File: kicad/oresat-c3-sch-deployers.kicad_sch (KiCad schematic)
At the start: 22 parts, among them Q10 FDMQ86530L, Q11 DMP2240UDM-7, Q5 DMP2240UDM-7, Q7 DMP2240UDM-7, Q8 FDMQ86530L, Q9 DMP2240UDM-7

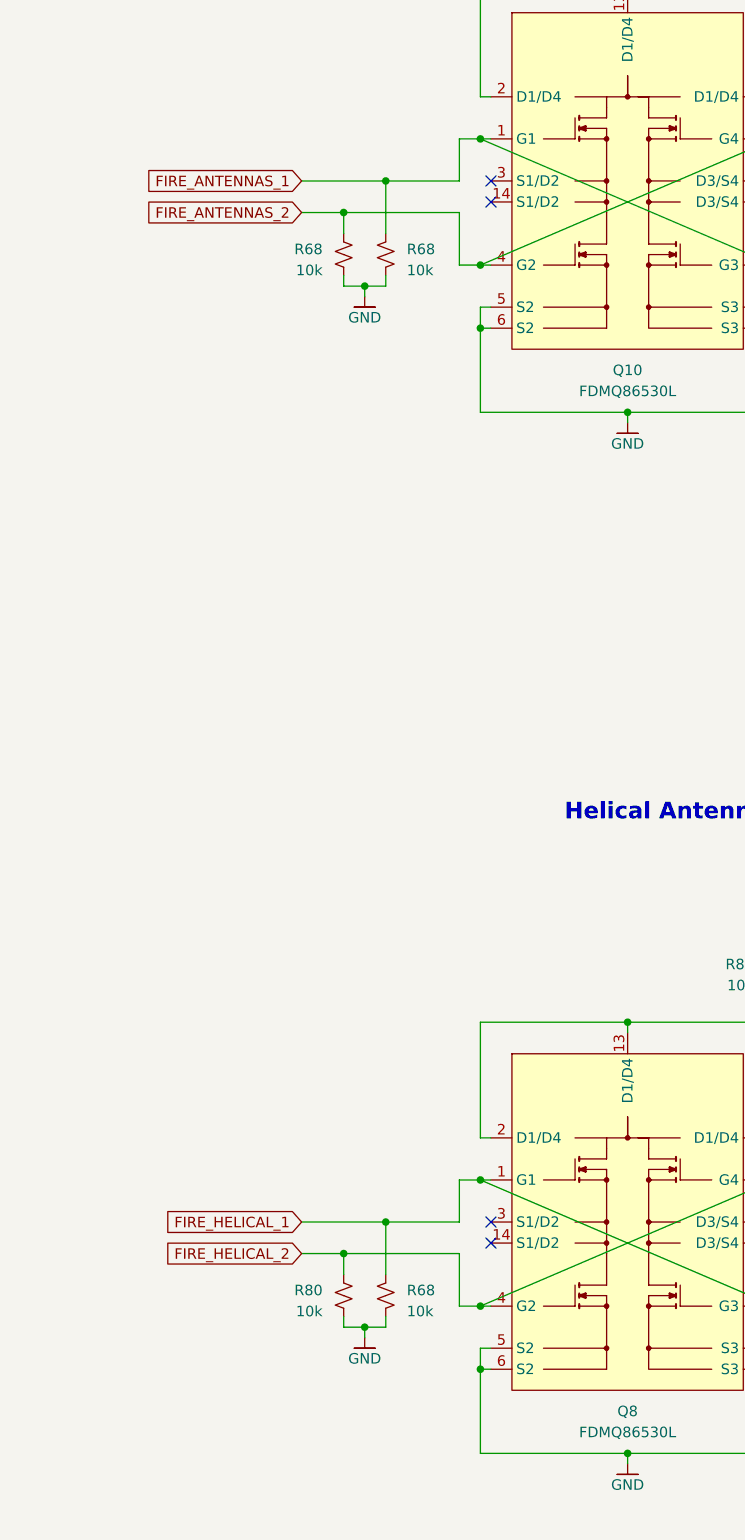
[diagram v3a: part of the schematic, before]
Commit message: Updated test points, fixed some more hidden ERCs.
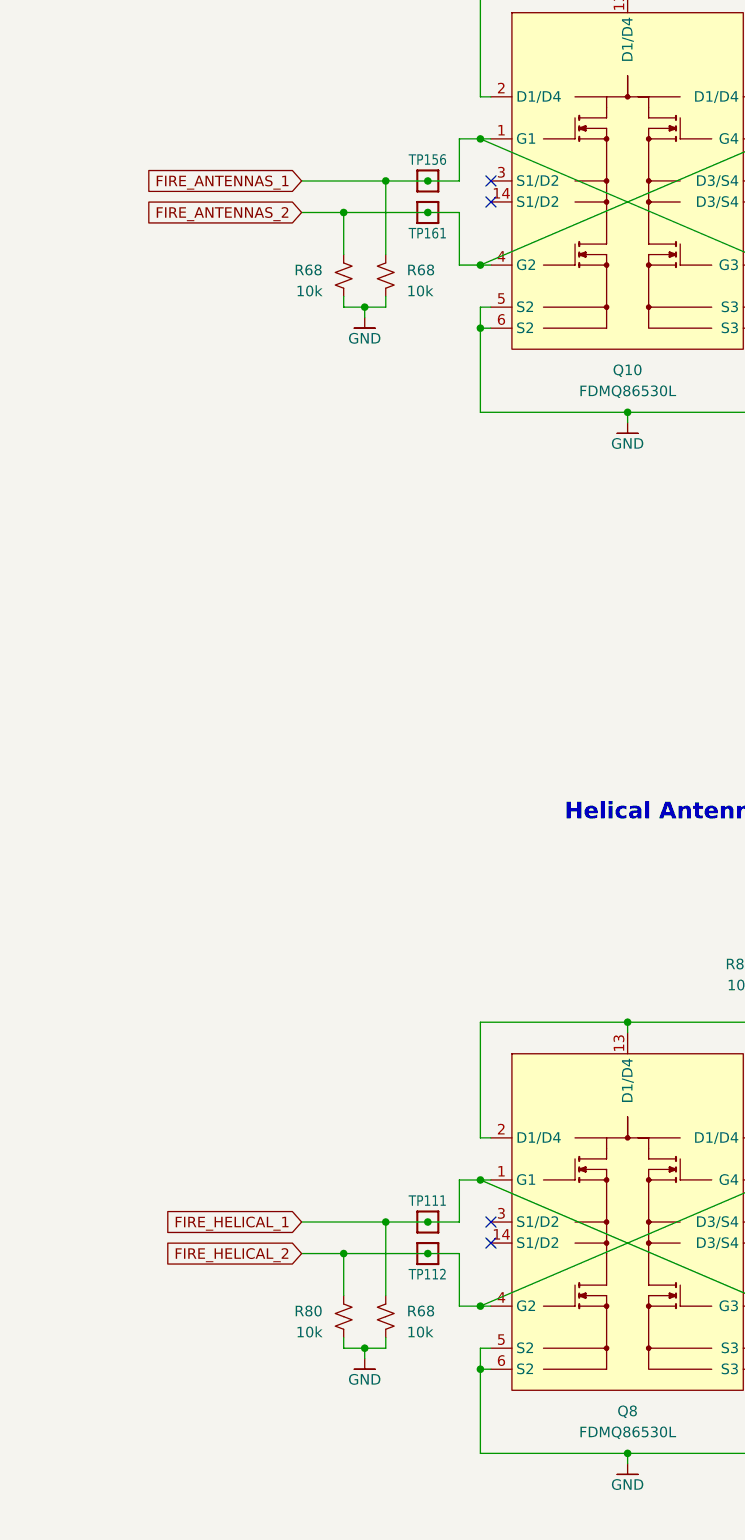
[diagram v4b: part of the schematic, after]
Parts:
- added TP111, TP112, TP156, TP161: Test-Point, TestPoint:TestPoint_Pad_D1.0mm, symbol oresat-misc:Test-Point-1mm-round
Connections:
- net FIRE_ANTENNAS_1: now also TP156.1
- net FIRE_ANTENNAS_2: now also TP161.1
- net FIRE_HELICAL_1: now also TP111.1
- net FIRE_HELICAL_2: now also TP112.1
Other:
- moved on the sheet: R68, R80

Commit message: Fixed test points; added RF test points. Started on layout and component packages for UHF radio.
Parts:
- TP1, TP111, TP112, TP156, TP161, TP3: footprint TestPoint:TestPoint_Pad_D1.0mm -> oresat-misc:TestPoint_Pad_D1.0mm
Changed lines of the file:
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@@
       (effects (font (size 1.27 1.27)) hide)
     )
-    (property "Footprint" "TestPoint:TestPoint_Pad_D1.0mm" (at 270.51 209.55 0)
+    (property "Footprint" "oresat-misc:TestPoint_Pad_D1.0mm" (at 270.51 209.55 0)
       (effects (font (size 1.27 1.27)) hide)
     )
@@
       (effects (font (size 1.27 1.27)) hide)
     )
-    (property "Footprint" "TestPoint:TestPoint_Pad_D1.0mm" (at 179.07 88.9 0)
+    (property "Footprint" "oresat-misc:TestPoint_Pad_D1.0mm" (at 179.07 88.9 0)
       (effects (font (size 1.27 1.27)) hide)
     )
@@
       (effects (font (size 1.27 1.27)) hide)
     )
-    (property "Footprint" "TestPoint:TestPoint_Pad_D1.0mm" (at 179.07 92.71 0)
+    (property "Footprint" "oresat-misc:TestPoint_Pad_D1.0mm" (at 179.07 92.71 0)
       (effects (font (size 1.27 1.27)) hide)
     )
@@
       (effects (font (size 1.27 1.27)) hide)
     )
-    (property "Footprint" "TestPoint:TestPoint_Pad_D1.0mm" (at 179.07 214.63 0)
+    (property "Footprint" "oresat-misc:TestPoint_Pad_D1.0mm" (at 179.07 214.63 0)
       (effects (font (size 1.27 1.27)) hide)
     )
@@
       (effects (font (size 1.27 1.27)) hide)
     )
-    (property "Footprint" "TestPoint:TestPoint_Pad_D1.0mm" (at 278.13 73.66 0)
+    (property "Footprint" "oresat-misc:TestPoint_Pad_D1.0mm" (at 278.13 73.66 0)
       (effects (font (size 1.27 1.27)) hide)
     )
@@
       (effects (font (size 1.27 1.27)) hide)
     )
-    (property "Footprint" "TestPoint:TestPoint_Pad_D1.0mm" (at 179.07 218.44 0)
-      (effects (font (size 1.27 1.27)) hide)
-    )
+    (property "Footprint" "oresat-misc:TestPoint_Pad_D1.0mm" (at 179.07 218.44 0)
+      (effects (font (size 1.27 1.27)) hide)
+    )

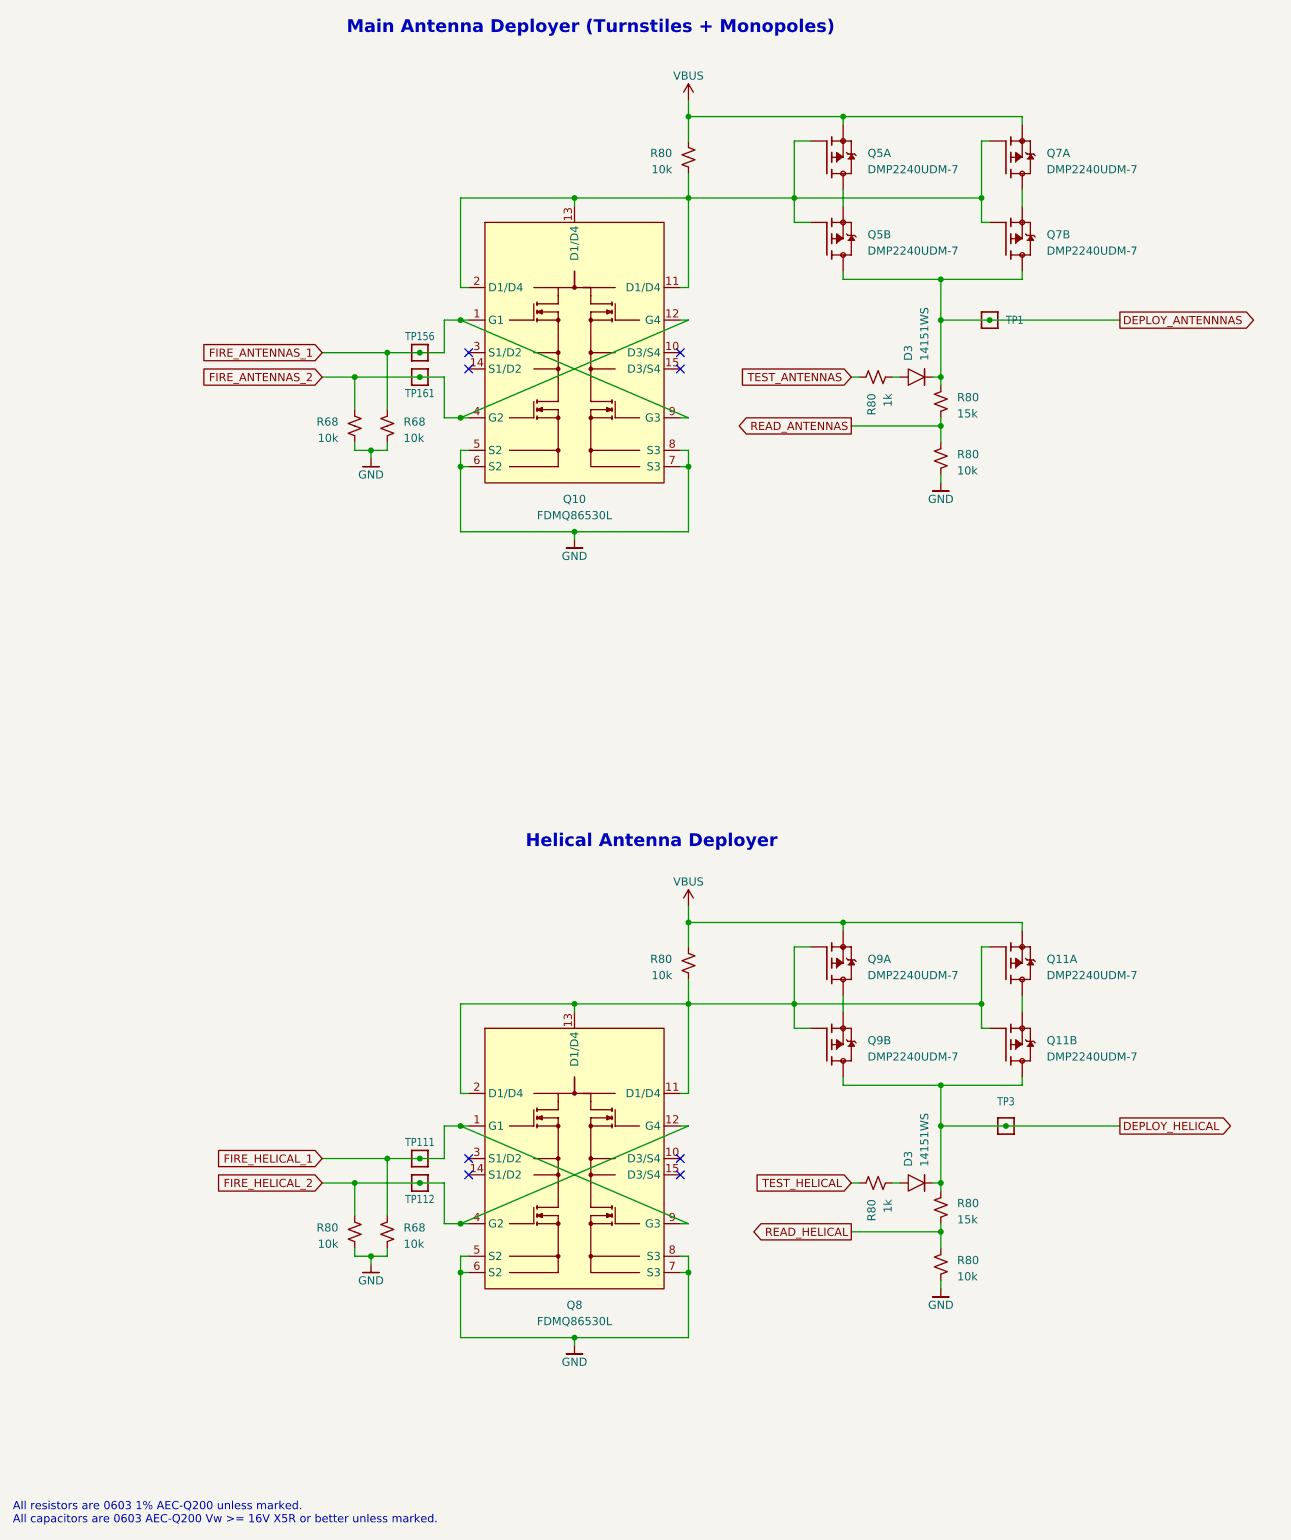
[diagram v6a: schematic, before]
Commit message: Fixed footprints and laid out WDT and OPD circuitry.
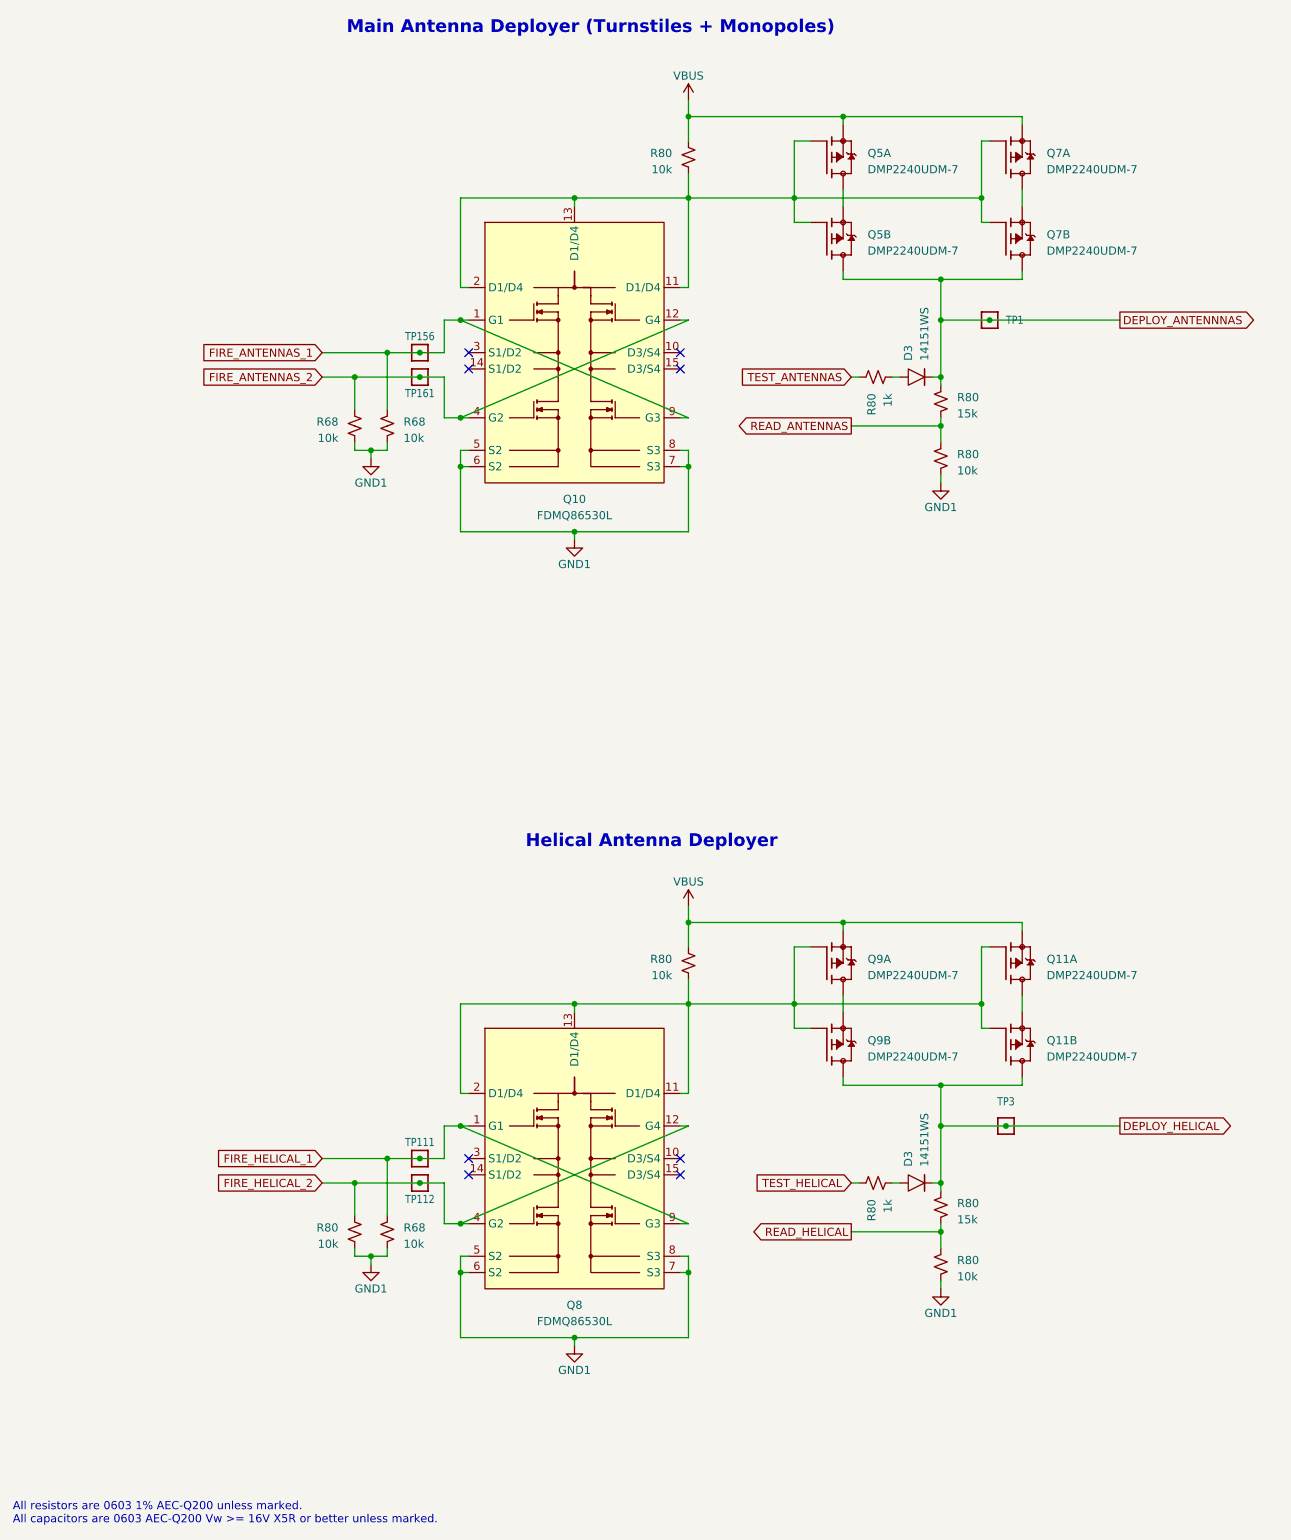
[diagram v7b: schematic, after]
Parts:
- R68, R80: footprint (none) -> Resistor_SMD:R_0603_1608Metric
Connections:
- net DEPLOY_ANTENNNAS: now also D3.1; no longer D3. (2)
- net DEPLOY_HELICAL: now also D3.1; no longer D3. (2)
- net at R80.2: now also D3.2; no longer D3. (2) (x2)
- net GND renamed GND1
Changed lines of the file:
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@@
     )
   )
-  (symbol (lib_id "oresat-power:GND") (at 171.45 95.25 0) (unit 1)
+  (symbol (lib_id "power:GND1") (at 171.45 95.25 0) (unit 1)
     (in_bom yes) (on_board yes) (dnp no)
     (property "Reference" "#GND0163" (at 171.45 101.6 0)
       (effects (font (size 1.27 1.27)) hide)
     )
-    (property "Value" "GND" (at 171.45 97.79 0)
+    (property "Value" "GND1" (at 171.45 99.06 0)
       (effects (font (size 1.27 1.27)))
     )
@@
         )
         (path "/65d12cdd-c326-4033-9053-c59fa4e0b25e/f40986af-661f-42e2-86b8-cadc1b813505"
-          (reference "#GND046") (unit 1)
+          (reference "#PWR0189") (unit 1)
         )
       )
@@
       (effects (font (size 1.27 1.27)) hide)
     )
-    (pin "")
-    (pin "")
+    (pin "1")
+    (pin "2")
     (instances
       (project "oresat-c3"
@@
       (effects (font (size 1.27 1.27)) (justify right))
     )
-    (property "Footprint" "" (at 220.98 173.99 0)
+    (property "Footprint" "Resistor_SMD:R_0603_1608Metric" (at 220.98 173.99 0)
       (effects (font (size 1.27 1.27)) hide)
     )
@@
     )
   )
-  (symbol (lib_id "oresat-power:GND") (at 171.45 220.98 0) (unit 1)
+  (symbol (lib_id "power:GND1") (at 171.45 220.98 0) (unit 1)
     (in_bom yes) (on_board yes) (dnp no)
     (property "Reference" "#GND0163" (at 171.45 227.33 0)
       (effects (font (size 1.27 1.27)) hide)
     )
-    (property "Value" "GND" (at 171.45 223.52 0)
+    (property "Value" "GND1" (at 171.45 224.79 0)
       (effects (font (size 1.27 1.27)))
     )
@@
         )
         (path "/65d12cdd-c326-4033-9053-c59fa4e0b25e/f40986af-661f-42e2-86b8-cadc1b813505"
-          (reference "#GND051") (unit 1)
+          (reference "#PWR0192") (unit 1)
         )
       )
@@
     )
   )
-  (symbol (lib_id "oresat-power:GND") (at 260.35 224.79 0) (unit 1)
+  (symbol (lib_id "power:GND1") (at 260.35 224.79 0) (unit 1)
     (in_bom yes) (on_board yes) (dnp no)
     (property "Reference" "#GND0163" (at 260.35 231.14 0)
       (effects (font (size 1.27 1.27)) hide)
     )
-    (property "Value" "GND" (at 260.35 227.33 0)
+    (property "Value" "GND1" (at 260.35 228.6 0)
       (effects (font (size 1.27 1.27)))
     )
@@
         )
         (path "/65d12cdd-c326-4033-9053-c59fa4e0b25e/f40986af-661f-42e2-86b8-cadc1b813505"
-          (reference "#GND053") (unit 1)
-        )
-      )
-    )
-  )
-  (symbol (lib_id "oresat-power:GND") (at 203.2 107.95 0) (unit 1)
+          (reference "#PWR0191") (unit 1)
+        )
+      )
+    )
+  )
+  (symbol (lib_id "power:GND1") (at 203.2 107.95 0) (unit 1)
     (in_bom yes) (on_board yes) (dnp no)
     (property "Reference" "#GND0163" (at 203.2 114.3 0)
       (effects (font (size 1.27 1.27)) hide)
     )
-    (property "Value" "GND" (at 203.2 110.49 0)
+    (property "Value" "GND1" (at 203.2 111.76 0)
       (effects (font (size 1.27 1.27)))
     )
@@
         )
         (path "/65d12cdd-c326-4033-9053-c59fa4e0b25e/f40986af-661f-42e2-86b8-cadc1b813505"
-          (reference "#GND049") (unit 1)
+          (reference "#PWR0190") (unit 1)
         )
       )
@@
       (effects (font (size 1.27 1.27)) (justify right))
     )
-    (property "Footprint" "" (at 250.19 208.28 0)
+    (property "Footprint" "Resistor_SMD:R_0603_1608Metric" (at 250.19 208.28 0)
       (effects (font (size 1.27 1.27)) hide)
     )
@@
       (effects (font (size 1.27 1.27)) (justify right))
     )
-    (property "Footprint" "" (at 173.99 90.17 0)
+    (property "Footprint" "Resistor_SMD:R_0603_1608Metric" (at 173.99 90.17 0)
       (effects (font (size 1.27 1.27)) hide)
     )
@@
       (effects (font (size 1.27 1.27)) (justify right))
     )
-    (property "Footprint" "" (at 220.98 48.26 0)
+    (property "Footprint" "Resistor_SMD:R_0603_1608Metric" (at 220.98 48.26 0)
       (effects (font (size 1.27 1.27)) hide)
     )
@@
       (effects (font (size 1.27 1.27)) (justify right))
     )
-    (property "Footprint" "" (at 260.35 86.36 0)
+    (property "Footprint" "Resistor_SMD:R_0603_1608Metric" (at 260.35 86.36 0)
       (effects (font (size 1.27 1.27)) hide)
     )
@@
       (effects (font (size 1.27 1.27)) (justify right))
     )
-    (property "Footprint" "" (at 260.35 220.98 0)
+    (property "Footprint" "Resistor_SMD:R_0603_1608Metric" (at 260.35 220.98 0)
       (effects (font (size 1.27 1.27)) hide)
     )
@@
       (effects (font (size 1.27 1.27)) (justify right))
     )
-    (property "Footprint" "" (at 168.91 90.17 0)
+    (property "Footprint" "Resistor_SMD:R_0603_1608Metric" (at 168.91 90.17 0)
       (effects (font (size 1.27 1.27)) hide)
     )
@@
       (effects (font (size 1.27 1.27)) (justify right))
     )
-    (property "Footprint" "" (at 260.35 212.09 0)
+    (property "Footprint" "Resistor_SMD:R_0603_1608Metric" (at 260.35 212.09 0)
       (effects (font (size 1.27 1.27)) hide)
     )
@@
       (effects (font (size 1.27 1.27)) hide)
     )
-    (pin "")
-    (pin "")
+    (pin "1")
+    (pin "2")
     (instances
       (project "oresat-c3"
@@
       (effects (font (size 1.27 1.27)) (justify right))
     )
-    (property "Footprint" "" (at 173.99 215.9 0)
+    (property "Footprint" "Resistor_SMD:R_0603_1608Metric" (at 173.99 215.9 0)
       (effects (font (size 1.27 1.27)) hide)
     )
@@
       (effects (font (size 1.27 1.27)) (justify right))
     )
-    (property "Footprint" "" (at 168.91 215.9 0)
+    (property "Footprint" "Resistor_SMD:R_0603_1608Metric" (at 168.91 215.9 0)
       (effects (font (size 1.27 1.27)) hide)
     )
@@
       (effects (font (size 1.27 1.27)) (justify right))
     )
-    (property "Footprint" "" (at 250.19 82.55 0)
+    (property "Footprint" "Resistor_SMD:R_0603_1608Metric" (at 250.19 82.55 0)
       (effects (font (size 1.27 1.27)) hide)
     )
@@
     )
   )
-  (symbol (lib_id "oresat-power:GND") (at 260.35 99.06 0) (unit 1)
+  (symbol (lib_id "power:GND1") (at 260.35 99.06 0) (unit 1)
     (in_bom yes) (on_board yes) (dnp no)
     (property "Reference" "#GND0163" (at 260.35 105.41 0)
       (effects (font (size 1.27 1.27)) hide)
     )
-    (property "Value" "GND" (at 260.35 101.6 0)
+    (property "Value" "GND1" (at 260.35 102.87 0)
       (effects (font (size 1.27 1.27)))
     )
@@
         )
         (path "/65d12cdd-c326-4033-9053-c59fa4e0b25e/f40986af-661f-42e2-86b8-cadc1b813505"
-          (reference "#GND050") (unit 1)
+          (reference "#PWR0187") (unit 1)
         )
       )
@@
       (effects (font (size 1.27 1.27)) (justify right))
     )
-    (property "Footprint" "" (at 260.35 95.25 0)
+    (property "Footprint" "Resistor_SMD:R_0603_1608Metric" (at 260.35 95.25 0)
       (effects (font (size 1.27 1.27)) hide)
     )
@@
     )
   )
-  (symbol (lib_id "oresat-power:GND") (at 203.2 233.68 0) (unit 1)
+  (symbol (lib_id "power:GND1") (at 203.2 233.68 0) (unit 1)
     (in_bom yes) (on_board yes) (dnp no)
     (property "Reference" "#GND0163" (at 203.2 240.03 0)
       (effects (font (size 1.27 1.27)) hide)
     )
-    (property "Value" "GND" (at 203.2 236.22 0)
+    (property "Value" "GND1" (at 203.2 237.49 0)
       (effects (font (size 1.27 1.27)))
     )
@@
         )
         (path "/65d12cdd-c326-4033-9053-c59fa4e0b25e/f40986af-661f-42e2-86b8-cadc1b813505"
-          (reference "#GND052") (unit 1)
-        )
-      )
+          (reference "#PWR0188") (unit 1)
+        )
+      )
